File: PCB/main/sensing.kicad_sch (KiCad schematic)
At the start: 9 parts, among them J6 Conn_01x02_Male, J7 Conn_01x02_Male, J8 Conn_01x02_Male, J9 Conn_01x02_Male, U2 DS18B20Z, U3 ALS-PDIC15-21B/TR8

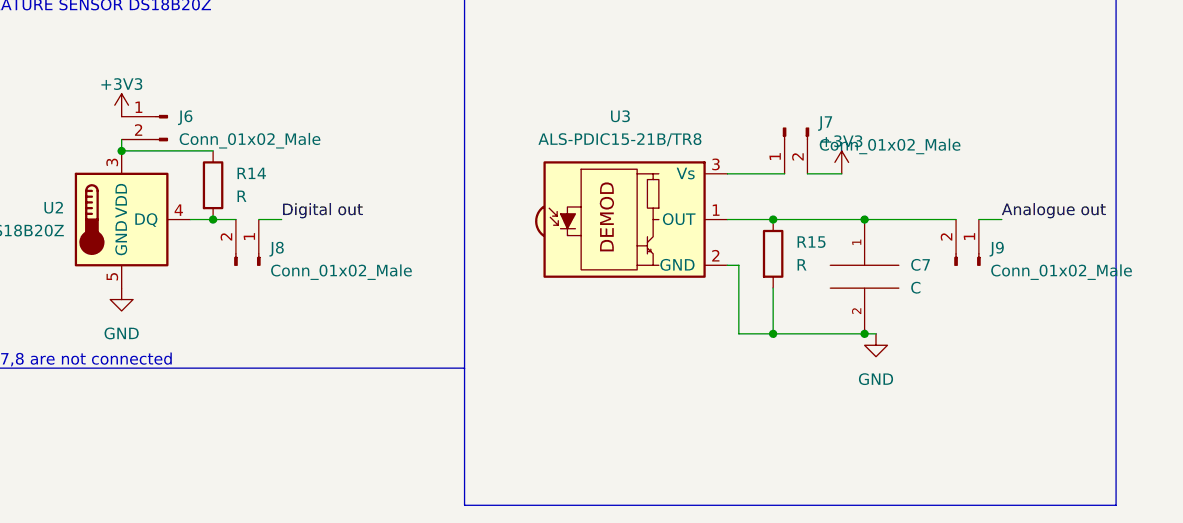
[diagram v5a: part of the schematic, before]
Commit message: Schematic updates
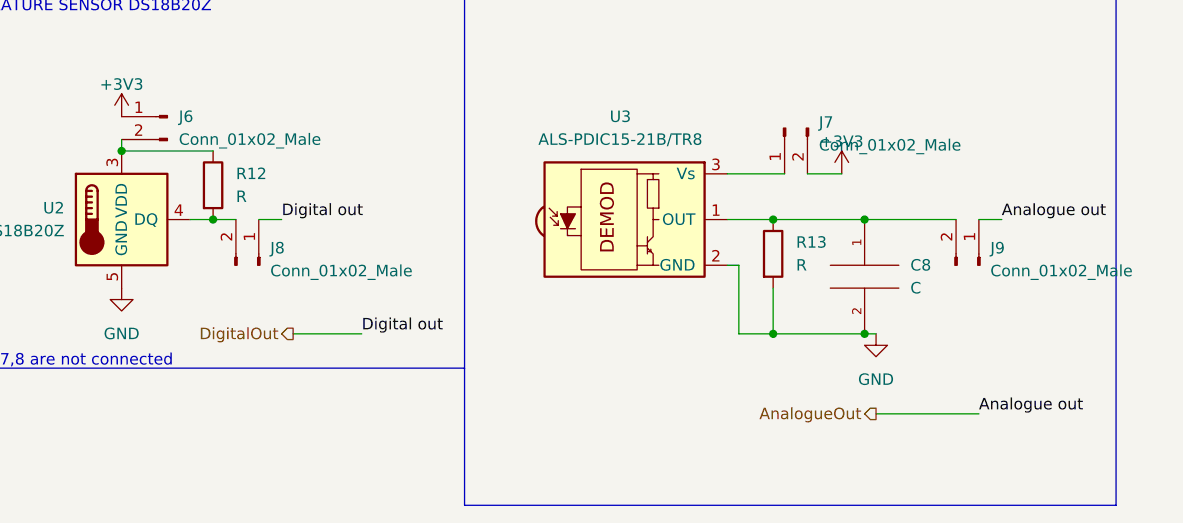
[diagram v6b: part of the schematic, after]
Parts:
- renumbered C7 to C8, R14 to R12, R15 to R13
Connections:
- net Analogue out renamed AnalogueOut
- net Digital out renamed DigitalOut
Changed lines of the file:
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@@
+    (stroke (width 0) (type default) (color 0 0 0 0))
+  )
+  (wire (pts (xy 191.77 146.05) (xy 199.39 146.05))
     (stroke (width 0) (type default) (color 0 0 0 0))
   )
@@
   )
   (polyline (pts (xy 143.51 106.68) (xy 283.21 106.68))
+    (stroke (width 0) (type default) (color 0 0 0 0))
+  )
+  (wire (pts (xy 256.54 154.94) (xy 267.97 154.94))
     (stroke (width 0) (type default) (color 0 0 0 0))
   )
@@
     (effects (font (size 1.27 1.27)) (justify left bottom))
   )
+  (label "Analogue out" (at 267.97 154.94 0)
+    (effects (font (size 1.27 1.27)) (justify left bottom))
+  )
   (label "Digital out" (at 190.5 133.35 0)
     (effects (font (size 1.27 1.27)) (justify left bottom))
+  )
+  (label "Digital out" (at 199.39 146.05 0)
+    (effects (font (size 1.27 1.27)) (justify left bottom))
+  )
+  (hierarchical_label "DigitalOut" (shape output) (at 191.77 146.05 180)
+    (effects (font (size 1.27 1.27)) (justify right))
+  )
+  (hierarchical_label "AnalogueOut" (shape output) (at 256.54 154.94 180)
+    (effects (font (size 1.27 1.27)) (justify right))
   )
   (symbol (lib_id "Sensor_Proximity:TSSP58038SS1XB") (at 229.87 133.35 0) (unit 1)
@@
   (symbol (lib_id "Device:R") (at 182.88 129.54 0) (unit 1)
     (in_bom yes) (on_board yes) (fields_autoplaced)
-    (property "Reference" "R14" (id 0) (at 185.42 128.2699 0)
+    (property "Reference" "R12" (id 0) (at 185.42 128.2699 0)
       (effects (font (size 1.27 1.27)) (justify left))
     )
@@
   (symbol (lib_id "power:GND") (at 256.54 146.05 0) (unit 1)
     (in_bom yes) (on_board yes) (fields_autoplaced)
-    (property "Reference" "#PWR039" (id 0) (at 256.54 152.4 0)
+    (property "Reference" "#PWR040" (id 0) (at 256.54 152.4 0)
       (effects (font (size 1.27 1.27)) hide)
     )
@@
   (symbol (lib_id "pspice:C") (at 255.27 139.7 0) (unit 1)
     (in_bom yes) (on_board yes)
-    (property "Reference" "C7" (id 0) (at 260.35 138.4299 0)
+    (property "Reference" "C8" (id 0) (at 260.35 138.4299 0)
       (effects (font (size 1.27 1.27)) (justify left))
     )
@@
   (symbol (lib_id "power:GND") (at 172.72 140.97 0) (unit 1)
     (in_bom yes) (on_board yes) (fields_autoplaced)
-    (property "Reference" "#PWR038" (id 0) (at 172.72 147.32 0)
+    (property "Reference" "#PWR039" (id 0) (at 172.72 147.32 0)
       (effects (font (size 1.27 1.27)) hide)
     )
@@
   (symbol (lib_id "power:+3V3") (at 252.73 128.27 0) (unit 1)
     (in_bom yes) (on_board yes) (fields_autoplaced)
-    (property "Reference" "#PWR037" (id 0) (at 252.73 132.08 0)
+    (property "Reference" "#PWR038" (id 0) (at 252.73 132.08 0)
       (effects (font (size 1.27 1.27)) hide)
     )
@@
   (symbol (lib_id "Device:R") (at 245.11 137.16 0) (unit 1)
     (in_bom yes) (on_board yes) (fields_autoplaced)
-    (property "Reference" "R15" (id 0) (at 247.65 135.8899 0)
+    (property "Reference" "R13" (id 0) (at 247.65 135.8899 0)
       (effects (font (size 1.27 1.27)) (justify left))
     )
@@
   (symbol (lib_id "power:+3V3") (at 172.72 121.92 0) (unit 1)
     (in_bom yes) (on_board yes) (fields_autoplaced)
-    (property "Reference" "#PWR036" (id 0) (at 172.72 125.73 0)
-      (effects (font (size 1.27 1.27)) hide)
-    )
+    (property "Reference" "#PWR037" (id 0) (at 172.72 125.73 0)
+      (effects (font (size 1.27 1.27)) hide)
+    )

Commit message: Power, uC, Sensing v0.1.1
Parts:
- C8: value C -> 10uF; footprint (none) -> 10uF_0804:CAPC2012X145N
- J6, J7, J8, J9: footprint (none) -> Connector_Molex:Molex_PicoBlade_53261-0271_1x02-1MP_P1.25mm_Horizontal
- R16: renamed from R12; value R -> 1k; footprint (none) -> 1k:RESC1608X55N
- R17: renamed from R13; value R -> 1k; footprint (none) -> 1k:RESC1608X55N
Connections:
- net +3V3 renamed 3V3

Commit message: Schematics v0.1.1 & PCB v0.01
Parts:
- J6, J7, J8, J9: footprint Connector_Molex:Molex_PicoBlade_53261-0271_1x02-1MP_P1.25mm_Horizontal -> conn_Molex_01_02_vert:53398-0271
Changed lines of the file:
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@@
   (symbol (lib_id "power:GND") (at 241.3 146.05 0) (unit 1)
     (in_bom yes) (on_board yes) (fields_autoplaced)
-    (property "Reference" "#PWR041" (id 0) (at 241.3 152.4 0)
+    (property "Reference" "#PWR042" (id 0) (at 241.3 152.4 0)
       (effects (font (size 1.27 1.27)) hide)
     )
@@
       (effects (font (size 1.27 1.27)) (justify left))
     )
-    (property "Footprint" "Connector_Molex:Molex_PicoBlade_53261-0271_1x02-1MP_P1.25mm_Horizontal" (id 2) (at 187.96 138.43 0)
+    (property "Footprint" "conn_Molex_01_02_vert:53398-0271" (id 2) (at 187.96 138.43 0)
       (effects (font (size 1.27 1.27)) hide)
     )
@@
       (effects (font (size 1.27 1.27)) (justify right))
     )
-    (property "Footprint" "Connector_Molex:Molex_PicoBlade_53261-0271_1x02-1MP_P1.25mm_Horizontal" (id 2) (at 177.8 121.92 0)
+    (property "Footprint" "conn_Molex_01_02_vert:53398-0271" (id 2) (at 177.8 121.92 0)
       (effects (font (size 1.27 1.27)) hide)
     )
@@
   (symbol (lib_id "power:GND") (at 172.72 142.24 0) (unit 1)
     (in_bom yes) (on_board yes) (fields_autoplaced)
-    (property "Reference" "#PWR040" (id 0) (at 172.72 148.59 0)
+    (property "Reference" "#PWR041" (id 0) (at 172.72 148.59 0)
       (effects (font (size 1.27 1.27)) hide)
     )
@@
       (effects (font (size 1.27 1.27)) (justify left))
     )
-    (property "Footprint" "Connector_Molex:Molex_PicoBlade_53261-0271_1x02-1MP_P1.25mm_Horizontal" (id 2) (at 267.97 138.43 0)
+    (property "Footprint" "conn_Molex_01_02_vert:53398-0271" (id 2) (at 267.97 138.43 0)
       (effects (font (size 1.27 1.27)) hide)
     )
@@
       (effects (font (size 1.27 1.27)) (justify right))
     )
-    (property "Footprint" "Connector_Molex:Molex_PicoBlade_53261-0271_1x02-1MP_P1.25mm_Horizontal" (id 2) (at 246.38 123.19 0)
+    (property "Footprint" "conn_Molex_01_02_vert:53398-0271" (id 2) (at 246.38 123.19 0)
       (effects (font (size 1.27 1.27)) hide)
     )
